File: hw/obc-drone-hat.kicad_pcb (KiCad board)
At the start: 4 copper layers, 65 x 56.5 mm, 68 parts, among them SW1 SW_DIP_x04

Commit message: hw: route dc-dc
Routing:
- net +5Vhat: track 0.00 -> 129.7 mm, vias 0 -> 14
- net GND: track 0.00 -> 86.5 mm, vias 0 -> 21
- net Vbat: track 0.00 -> 44.1 mm, vias 0 -> 15
- net /RPi/ID_SCL: track 0.00 -> 15.4 mm
- net /DC-DC/CB: track 0.00 -> 12.1 mm
- net +3.3VP: track 0.00 -> 11.0 mm
- net /RPi/ID_SDA: track 0.00 -> 9.71 mm
- net +5VP: track 0.00 -> 2.90 mm
- net ~HAT_ID_WE: track 0.00 -> 2.81 mm
- net ~STM_RESET: track 0.00 -> 1.45 mm
- net ~STM_INT: track 0.00 -> 1.45 mm
- net ~SER_IRQ: track 0.00 -> 1.45 mm
- net ~RPI_SPI0_CE1: track 0.00 -> 1.45 mm
- net ~RPI_SPI0_CE0: track 0.00 -> 1.45 mm
- net STM_BOOT0: track 0.00 -> 1.45 mm
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- added copper zone on F.Cu, net /DC-DC/VSW
- added copper zone on F.Cu, net Vbat
- added copper zone on In1.Cu, net Vbat
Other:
- net class Default: trace_width 0.25 -> 0.2; via_drill 0.4 -> 0.3
- rule trace_min: 0.2 -> 0.15
- rule via_min_size: 0.4 -> 0.3

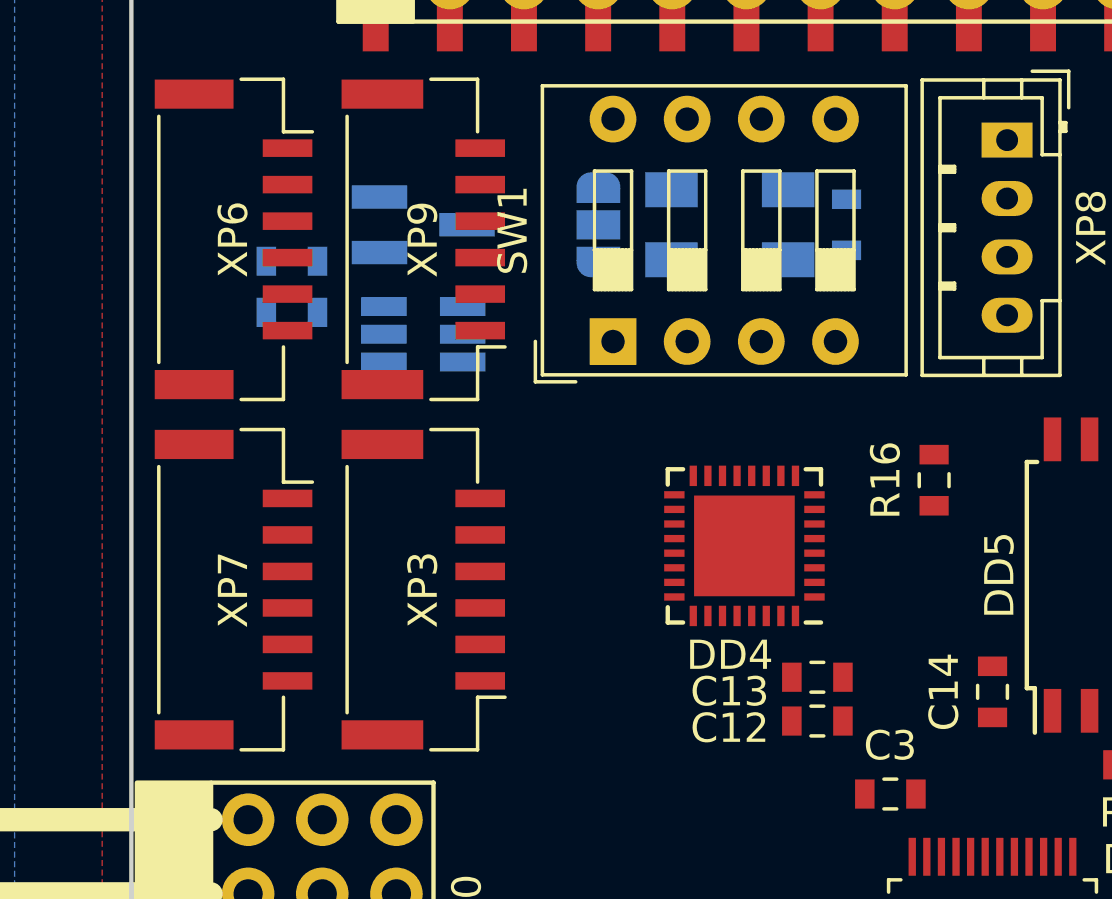
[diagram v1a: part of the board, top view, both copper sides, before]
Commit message: hw: route telem uarts
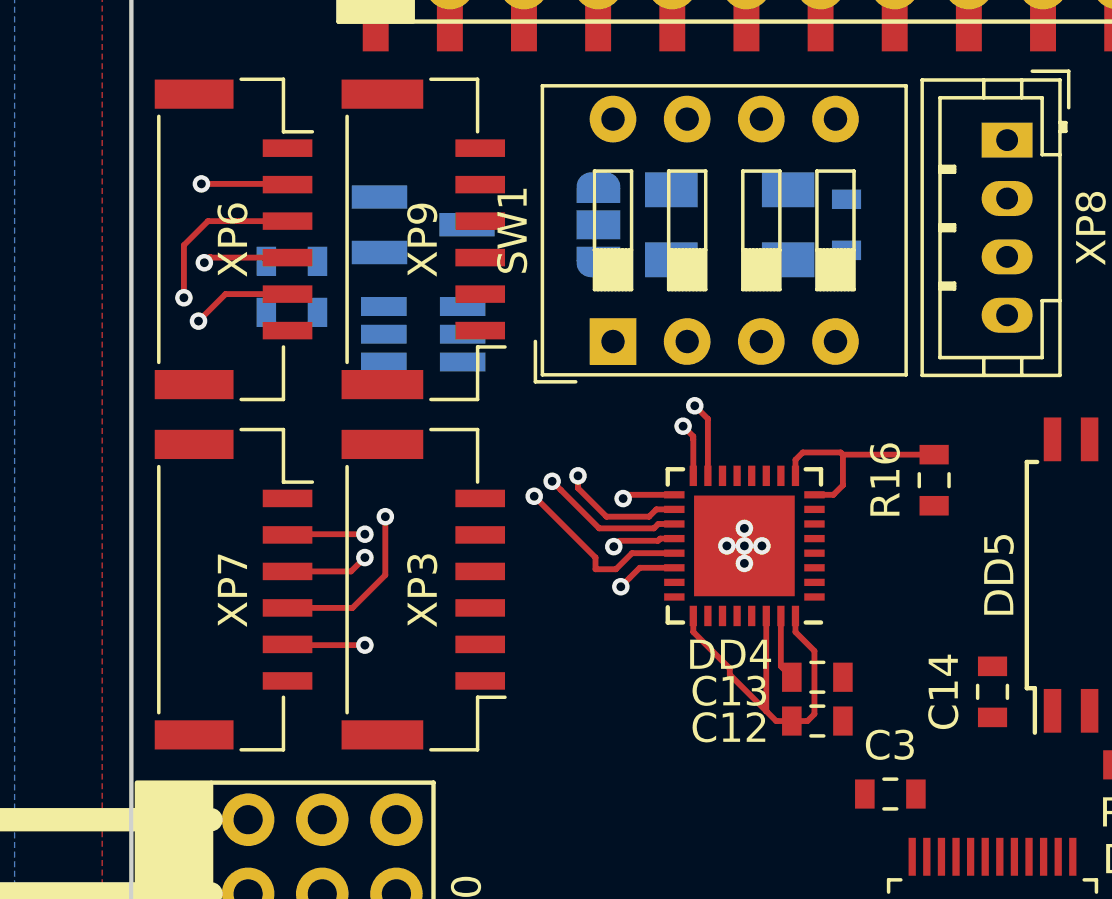
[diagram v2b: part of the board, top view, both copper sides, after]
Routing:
- net /UART/U0_TX: track 0.00 -> 27.1 mm, vias 0 -> 2
- net /UART/U0_RX: track 0.00 -> 25.8 mm, vias 0 -> 2
- net /UART/~U0_CTX: track 0.00 -> 24.4 mm, vias 0 -> 2
- net /UART/~U0_RTS: track 0.00 -> 23.7 mm, vias 0 -> 2
- net +3.3VP: track 11.0 -> 31.6 mm
- net /UART/~U1_CTX: track 0.00 -> 19.1 mm, vias 0 -> 2
- net /UART/~U1_RTS: track 0.00 -> 14.4 mm, vias 0 -> 2
- net /UART/U1_TX: track 0.00 -> 13.8 mm, vias 0 -> 2
- net /UART/U1_RX: track 0.00 -> 13.7 mm, vias 0 -> 2
- net /UART/U_V18: track 0.00 -> 2.26 mm
- net GND: vias 21 -> 26

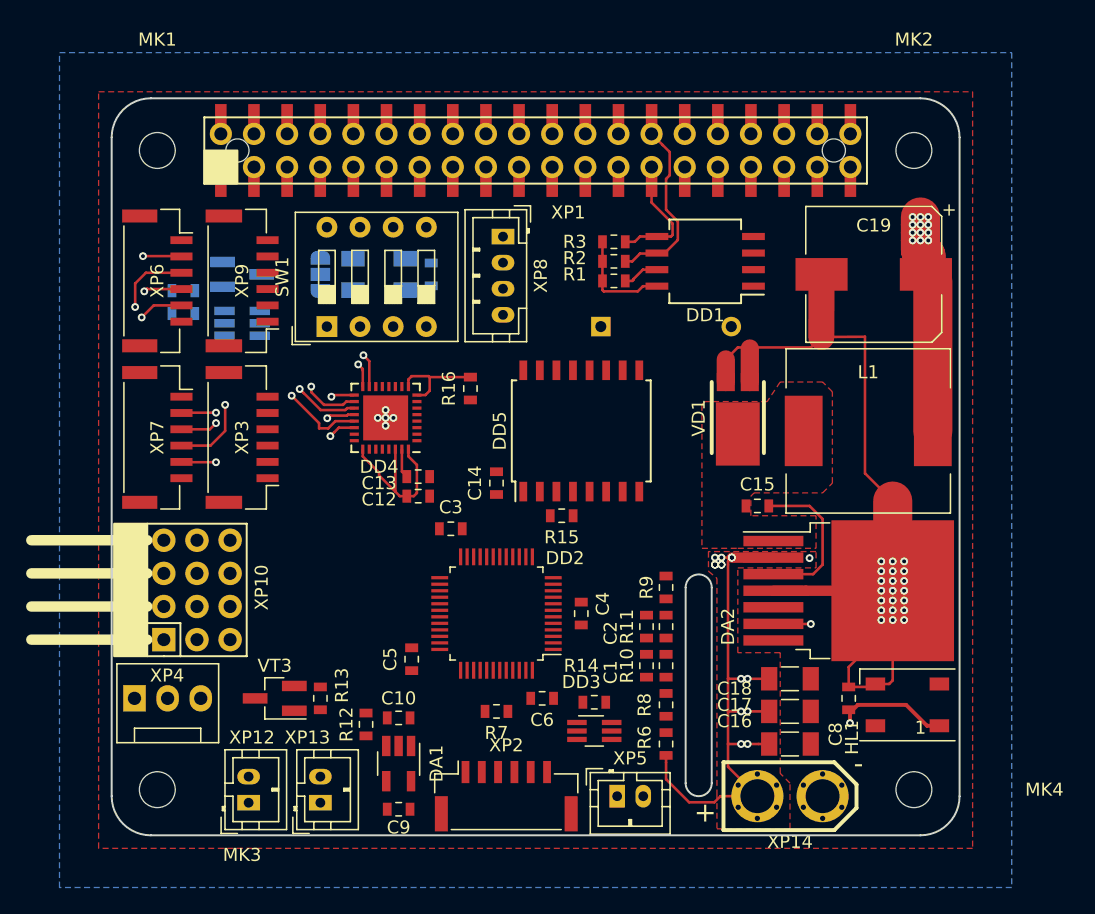
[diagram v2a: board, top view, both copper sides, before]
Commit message: hw: route stm debug port
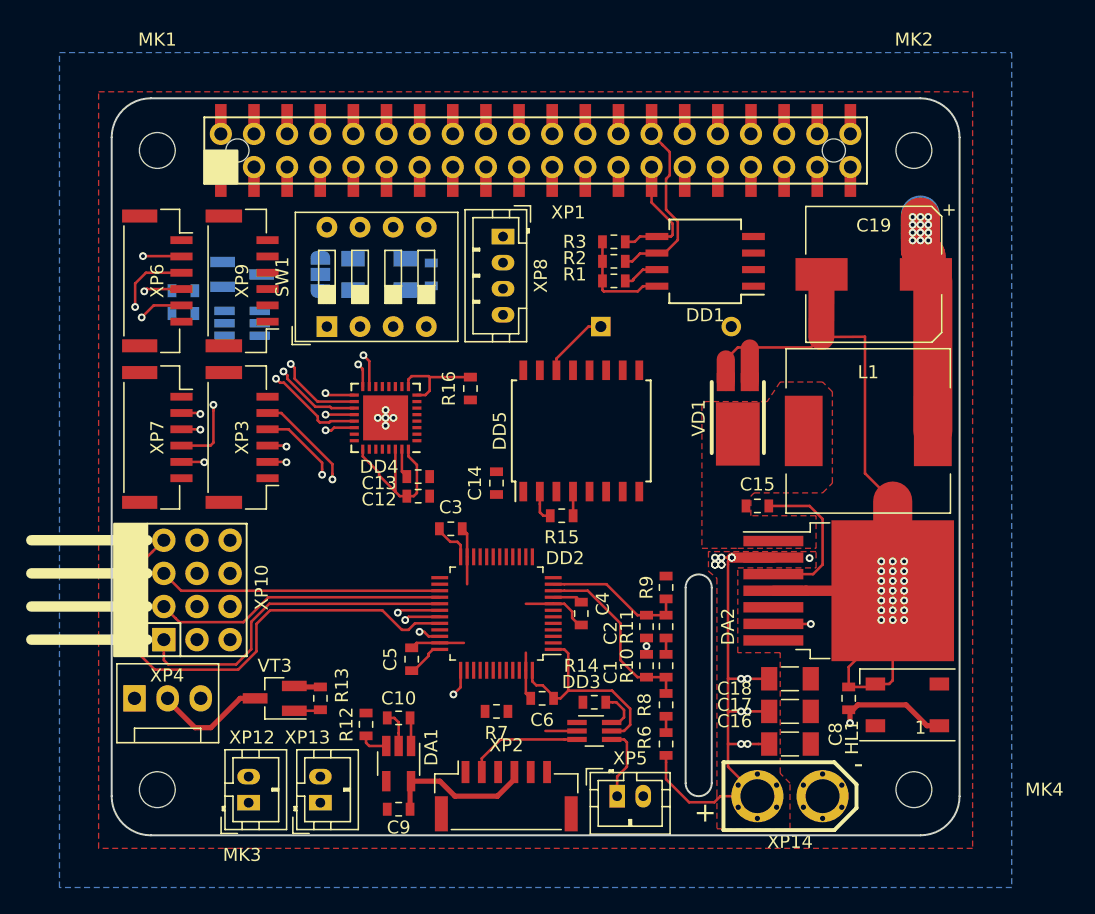
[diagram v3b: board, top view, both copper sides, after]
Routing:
- net GND: track 86.5 -> 126.1 mm, vias 26 -> 27
- net SERVO3: track 0.00 -> 36.9 mm
- net /RC IO MCU/SWCLK: track 0.00 -> 30.7 mm, vias 0 -> 2
- net +3.3VP: track 31.6 -> 59.3 mm
- net SERVO0: track 0.00 -> 26.0 mm
- net /RC IO MCU/SWDIO: track 0.00 -> 23.6 mm, vias 0 -> 2
- net SERVO1: track 0.00 -> 22.4 mm
- net SERVO2: track 0.00 -> 21.7 mm
- net /RC IO MCU/STM_U1_RX: track 0.00 -> 21.6 mm, vias 0 -> 2
- net /RC IO MCU/STM_U1_TX: track 0.00 -> 19.8 mm, vias 0 -> 2
- net /RC IO MCU/ADC_IN0_Vbat: track 0.00 -> 14.3 mm
- net /RC IO MCU/Rx_5V: track 0.00 -> 11.7 mm
- net /RC IO MCU/ADC_IN1_5V: track 0.00 -> 10.9 mm
- net /RC IO MCU/Rx_CPPM: track 0.00 -> 8.95 mm
- net /RC IO MCU/FAN+: track 0.00 -> 8.66 mm
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
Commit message: hw: route pi 5vp
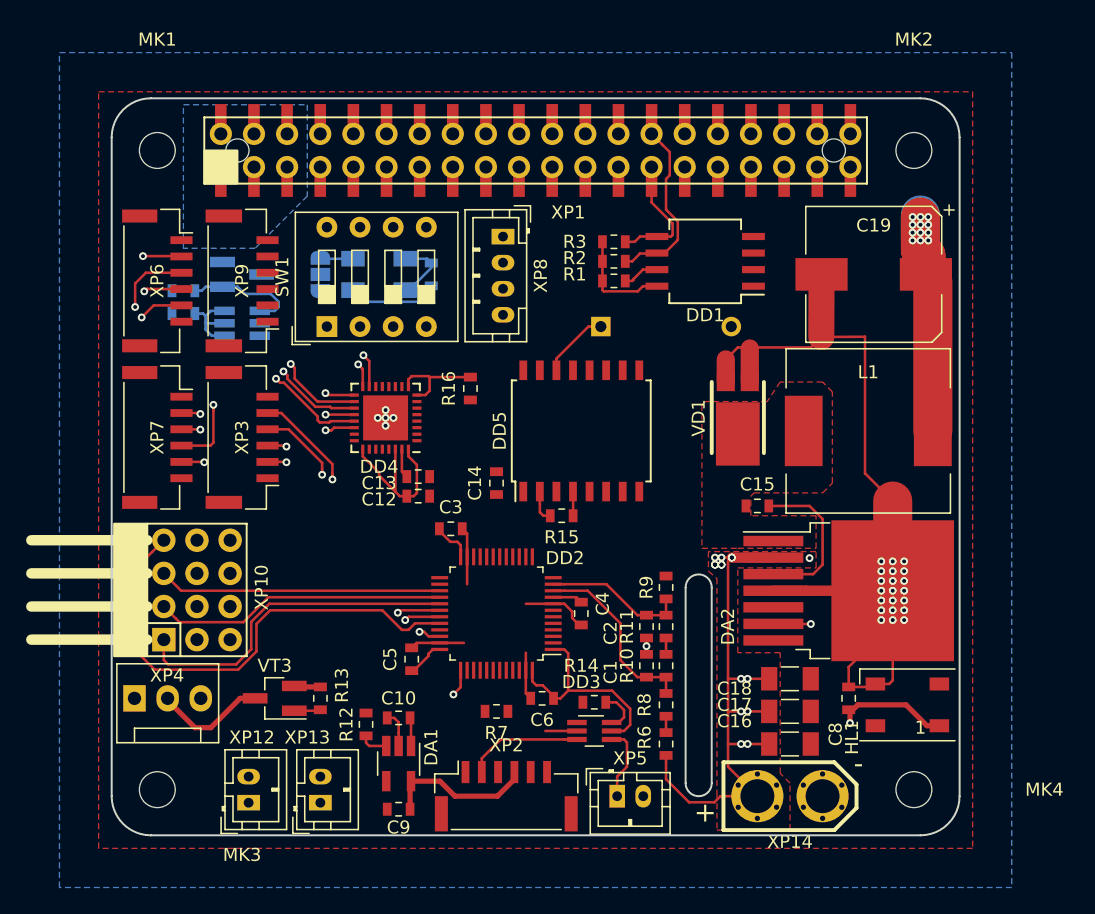
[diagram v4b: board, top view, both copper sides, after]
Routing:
- net /RPi/ZVD_G: track 0.00 -> 9.00 mm
- net GND: track 126.1 -> 133.8 mm
- net /RPi/ZVD_B: track 0.00 -> 6.67 mm
- net +3.3VP: track 59.3 -> 64.5 mm
- net /UART/ZQ_CLK: track 0.00 -> 2.54 mm
- added copper zone on B.Cu, net +5VP
- added copper zone on In1.Cu, net +5VP
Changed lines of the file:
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@@
     (thickness 1.6)
     (drawings 22)
-    (tracks 556)
+    (tracks 588)
     (zones 0)
     (modules 68)
@@
   (segment (start 139.08 125) (end 139.08 128.17) (width 2) (layer In2.Cu) (net 1))
   (segment (start 139.08 117.38) (end 139.08 113.67) (width 2) (layer In2.Cu) (net 1))
+  (segment (start 154.5 98.41) (end 154.5 97.875) (width 0.2) (layer B.Cu) (net 1))
+  (segment (start 153.809999 99.100001) (end 154.5 98.41) (width 0.2) (layer B.Cu) (net 1))
+  (segment (start 148.600001 99.100001) (end 153.809999 99.100001) (width 0.2) (layer B.Cu) (net 1))
+  (segment (start 148.5 99) (end 148.600001 99.100001) (width 0.2) (layer B.Cu) (net 1))
+  (segment (start 148.5 98.2) (end 148.5 99) (width 0.2) (layer B.Cu) (net 1))
   (segment (start 172.5 129.125) (end 172.5 127.875) (width 0.2) (layer F.Cu) (net 2))
   (segment (start 172.5 127.875) (end 171 127.875) (width 0.2) (layer F.Cu) (net 2))
@@
   (segment (start 169.75 130.299998) (end 168.360002 128.91) (width 0.2) (layer F.Cu) (net 4))
   (segment (start 169.75 131.53) (end 169.75 130.299998) (width 0.2) (layer F.Cu) (net 4))
+  (segment (start 154.175 95.8) (end 154.5 96.125) (width 0.2) (layer B.Cu) (net 4))
+  (segment (start 152.5 95.8) (end 154.175 95.8) (width 0.2) (layer B.Cu) (net 4))
+  (segment (start 154.5 96.5) (end 154.5 96.125) (width 0.2) (layer B.Cu) (net 4))
+  (segment (start 152.8 98.2) (end 154.5 96.5) (width 0.2) (layer B.Cu) (net 4))
+  (segment (start 152.5 98.2) (end 152.8 98.2) (width 0.2) (layer B.Cu) (net 4))
   (segment (start 152.875 135.925) (end 152.95 135.85) (width 0.2) (layer F.Cu) (net 5))
   (segment (start 152.875 138) (end 152.875 135.925) (width 0.4) (layer F.Cu) (net 5))
@@
   (segment (start 168.75 135.5) (end 168.75 137) (width 0.2) (layer F.Cu) (net 31))
   (segment (start 169.5 134.75) (end 168.75 135.5) (width 0.2) (layer F.Cu) (net 31))
+  (segment (start 146.1 95.8) (end 146 95.7) (width 0.2) (layer B.Cu) (net 32))
+  (segment (start 148.5 95.8) (end 146.1 95.8) (width 0.2) (layer B.Cu) (net 32))
   (segment (start 145.99 88.77) (end 145.99 90.22) (width 0.2) (layer F.Cu) (net 33) (status 30))
   (segment (start 172.5 132.125) (end 172.5 130.875) (width 0.2) (layer F.Cu) (net 34))
@@
   (segment (start 142.1471 122.75) (end 141.099991 123.797109) (width 0.2) (layer F.Cu) (net 52))
   (segment (start 153.25 123.75) (end 152.75 124.25) (width 0.2) (layer F.Cu) (net 52))
+  (segment (start 137 100) (end 136.375 100) (width 0.2) (layer B.Cu) (net 53))
+  (segment (start 137.2 100.2) (end 137 100) (width 0.2) (layer B.Cu) (net 53))
+  (segment (start 138.65 101.7) (end 137.67 101.7) (width 0.2) (layer B.Cu) (net 53))
+  (segment (start 137.67 101.7) (end 137.2 101.23) (width 0.2) (layer B.Cu) (net 53))
+  (segment (start 137.6 99.8) (end 137.2 100.2) (width 0.2) (layer B.Cu) (net 53))
+  (segment (start 138.65 99.8) (end 137.6 99.8) (width 0.2) (layer B.Cu) (net 53))
+  (segment (start 137.25 100.75) (end 137.2 100.7) (width 0.2) (layer B.Cu) (net 53))
+  (segment (start 138.65 100.75) (end 137.25 100.75) (width 0.2) (layer B.Cu) (net 53))
+  (segment (start 137.2 101.23) (end 137.2 100.7) (width 0.2) (layer B.Cu) (net 53))
+  (segment (start 137.2 100.7) (end 137.2 100.2) (width 0.2) (layer B.Cu) (net 53))
+  (segment (start 137.21 97.95) (end 138.5 97.95) (width 0.2) (layer B.Cu) (net 54))
+  (segment (start 136.375 98.25) (end 136.91 98.25) (width 0.2) (layer B.Cu) (net 54))
+  (segment (start 136.91 98.25) (end 137.21 97.95) (width 0.2) (layer B.Cu) (net 54))
+  (segment (start 139.65 97.95) (end 138.5 97.95) (width 0.2) (layer B.Cu) (net 54))
+  (segment (start 141.35 99.8) (end 142.5 99.8) (width 0.2) (layer B.Cu) (net 54))
+  (segment (start 140.2 98.5) (end 139.65 97.95) (width 0.2) (layer B.Cu) (net 54))
+  (segment (start 142.8 99.5) (end 142.8 99.1) (width 0.2) (layer B.Cu) (net 54))
+  (segment (start 142.5 99.8) (end 142.8 99.5) (width 0.2) (layer B.Cu) (net 54))
+  (segment (start 142.8 99.1) (end 142.2 98.5) (width 0.2) (layer B.Cu) (net 54))
+  (segment (start 142.2 98.5) (end 140.2 98.5) (width 0.2) (layer B.Cu) (net 54))
   (zone (net 1) (net_name GND) (layer F.Cu) (hatch edge 0.508)
-    (connect_pads (clearance 0.508))
-    (min_thickness 0.254)
-    (fill yes (arc_segments 16) (thermal_gap 0.508) (thermal_bridge_width 0.508))
+    (connect_pads (clearance 0.3))
+    (min_thickness 0.2)
+    (fill yes (arc_segments 32) (thermal_gap 0.3) (thermal_bridge_width 0.5))
     (polygon
       (pts
@@
     (connect_pads (clearance 0.3))
     (min_thickness 0.2)
-    (fill yes (arc_segments 16) (thermal_gap 0.508) (thermal_bridge_width 0.508))
+    (fill yes (arc_segments 32) (thermal_gap 0.3) (thermal_bridge_width 0.5))
     (polygon
       (pts
@@
   )
   (zone (net 1) (net_name GND) (layer In2.Cu) (hatch edge 0.508)
-    (connect_pads (clearance 0.508))
-    (min_thickness 0.254)
-    (fill yes (arc_segments 16) (thermal_gap 0.508) (thermal_bridge_width 0.508))
+    (connect_pads (clearance 0.3))
+    (min_thickness 0.2)
+    (fill yes (arc_segments 32) (thermal_gap 0.3) (thermal_bridge_width 0.5))
     (polygon
       (pts
@@
   )
   (zone (net 1) (net_name GND) (layer B.Cu) (hatch edge 0.508)
-    (connect_pads (clearance 0.508))
-    (min_thickness 0.254)
-    (fill yes (arc_segments 16) (thermal_gap 0.508) (thermal_bridge_width 0.508))
+    (connect_pads (clearance 0.3))
+    (min_thickness 0.2)
+    (fill yes (arc_segments 32) (thermal_gap 0.3) (thermal_bridge_width 0.5))
     (polygon
       (pts
@@
     (connect_pads (clearance 0.15))
     (min_thickness 0.15)
-    (fill yes (mode segment) (arc_segments 16) (thermal_gap 0.2) (thermal_bridge_width 2))
+    (fill yes (mode segment) (arc_segments 32) (thermal_gap 0.2) (thermal_bridge_width 2))
     (polygon
       (pts
         (xy 181.25 135.25) (xy 181.25 126) (xy 178 126) (xy 178 119.5) (xy 184 119.5)
         (xy 184 118.25) (xy 175.75 118.25) (xy 175.75 119.75) (xy 176.4 120.3) (xy 176.4 136.8)
-        (xy 176.4 139.5) (xy 182 139.5) (xy 182 136)
+        (xy 176.4 139.6) (xy 182 139.6) (xy 182 136)
       )
     )
@@
     (connect_pads yes (clearance 0.15))
     (min_thickness 0.15)
-    (fill yes (mode segment) (arc_segments 16) (thermal_gap 0.2) (thermal_bridge_width 2))
+    (fill yes (mode segment) (arc_segments 32) (thermal_gap 0.2) (thermal_bridge_width 2))
     (polygon
       (pts
         (xy 181.25 135.25) (xy 181.25 126.55) (xy 181.8 126) (xy 181.8 120.3) (xy 184 119.5)
         (xy 184 118.25) (xy 175.75 118.25) (xy 175.75 119.75) (xy 176.4 120.3) (xy 176.4 136.7)
-        (xy 176.4 139.5) (xy 182 139.5) (xy 182 136)
+        (xy 176.4 139.6) (xy 182 139.6) (xy 182 136)
       )
     )
@@
     (connect_pads yes (clearance 0.5))
     (min_thickness 0.15)
-    (fill yes (mode segment) (arc_segments 16) (thermal_gap 0.2) (thermal_bridge_width 3))
+    (fill yes (mode segment) (arc_segments 32) (thermal_gap 0.2) (thermal_bridge_width 3))
+    (polygon
+      (pts
+        (xy 176.8 139.2) (xy 176.8 133.9) (xy 190.5 133.9) (xy 190.5 139.5) (xy 177.4 139.5)
+      )
+    )
+  )
+  (zone (net 6) (net_name +5VP) (layer B.Cu) (hatch edge 0.508)
+    (priority 2)
+    (connect_pads (clearance 0.3))
+    (min_thickness 0.2)
+    (fill yes (mode segment) (arc_segments 32) (thermal_gap 0.3) (thermal_bridge_width 0.8))
+    (polygon
+      (pts
+        (xy 135.5 84) (xy 145 84) (xy 145 91) (xy 141 95) (xy 135.5 95)
+      )
+    )
+  )
+  (zone (net 6) (net_name +5VP) (layer In1.Cu) (hatch edge 0.508)
+    (priority 2)
+    (connect_pads (clearance 0.2))
+    (min_thickness 0.2)
+    (fill yes (mode segment) (arc_segments 32) (thermal_gap 0.2) (thermal_bridge_width 0.8))
     (polygon
       (pts
-        (xy 176.8 139.2) (xy 176.8 133.4) (xy 189.5 133.4) (xy 189.5 139.5) (xy 177.4 139.5)
+        (xy 135.5 84) (xy 145 84) (xy 145 91) (xy 141 95) (xy 135.5 95)
       )
     )
